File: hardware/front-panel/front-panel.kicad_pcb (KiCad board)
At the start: 4 copper layers, 180 x 100 mm, 78 parts, among them J1 Panel link 2x20 female, J10 SMA, J11 SMA, J12 SMA, J13 SMA, J14 SMA, J15 SMA, J16 SMA, J17 SMA, J18 SMA, J19 SMA, J2 Panel link 2x20 female, J20 SMA, J21 SMA, J22 SMA, J23 SMA, J24 SMA, J25 SMA, J26 SMA, J3 Panel link 2x20 female, J30 OLED 0.96in module on 1x4 soc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, J31 KF128-2.54-10P, J32 KF128-5.0-2P, J33 Qwiic (vertical), J40 Module header 2x6 (shrouded), J411 KF301-5.0-2P, J412 KF301-5.0-2P, Q411 MMBT5551, Q412 MMBT5551, Q421 MMBT5551, Q422 MMBT5551, U401 6N137S-TA1-L, U402 6N137S-TA1-L, U410 SN74AHCT541PWR

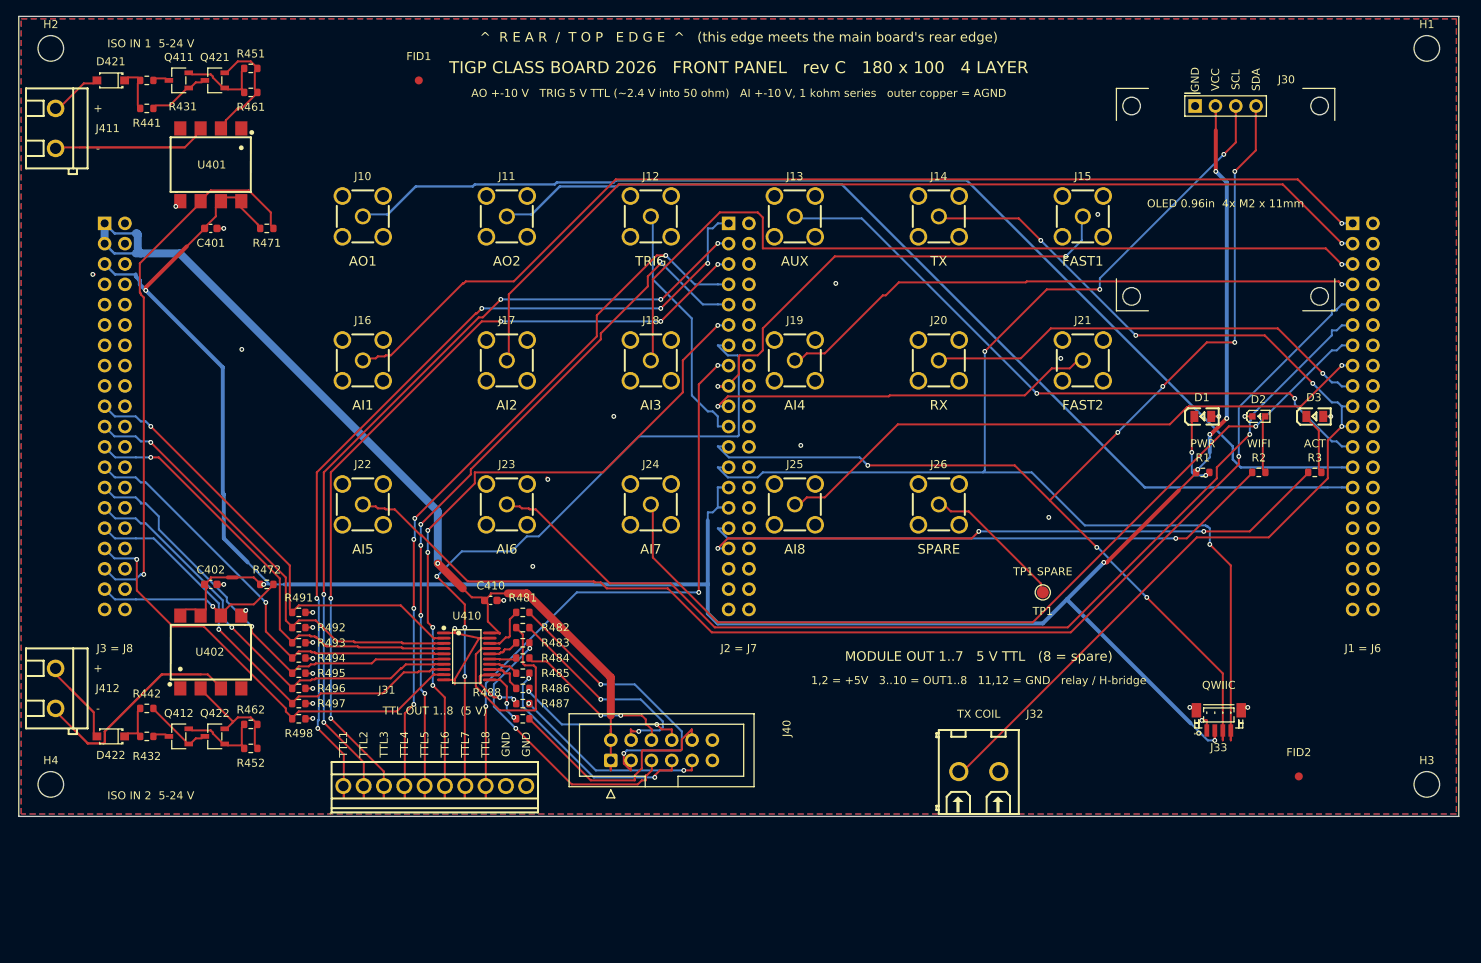
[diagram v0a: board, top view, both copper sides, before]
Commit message: front panel: OLED footprint per the real module (27 x 29 mm, holes 24 x 26 mm, header 1 mm below the top edge), panel + student copy regenerated, DRC 0/0 with zones filled
Co-Authored-By: Claude Fable 5.1 <noreply@anthropic.com>
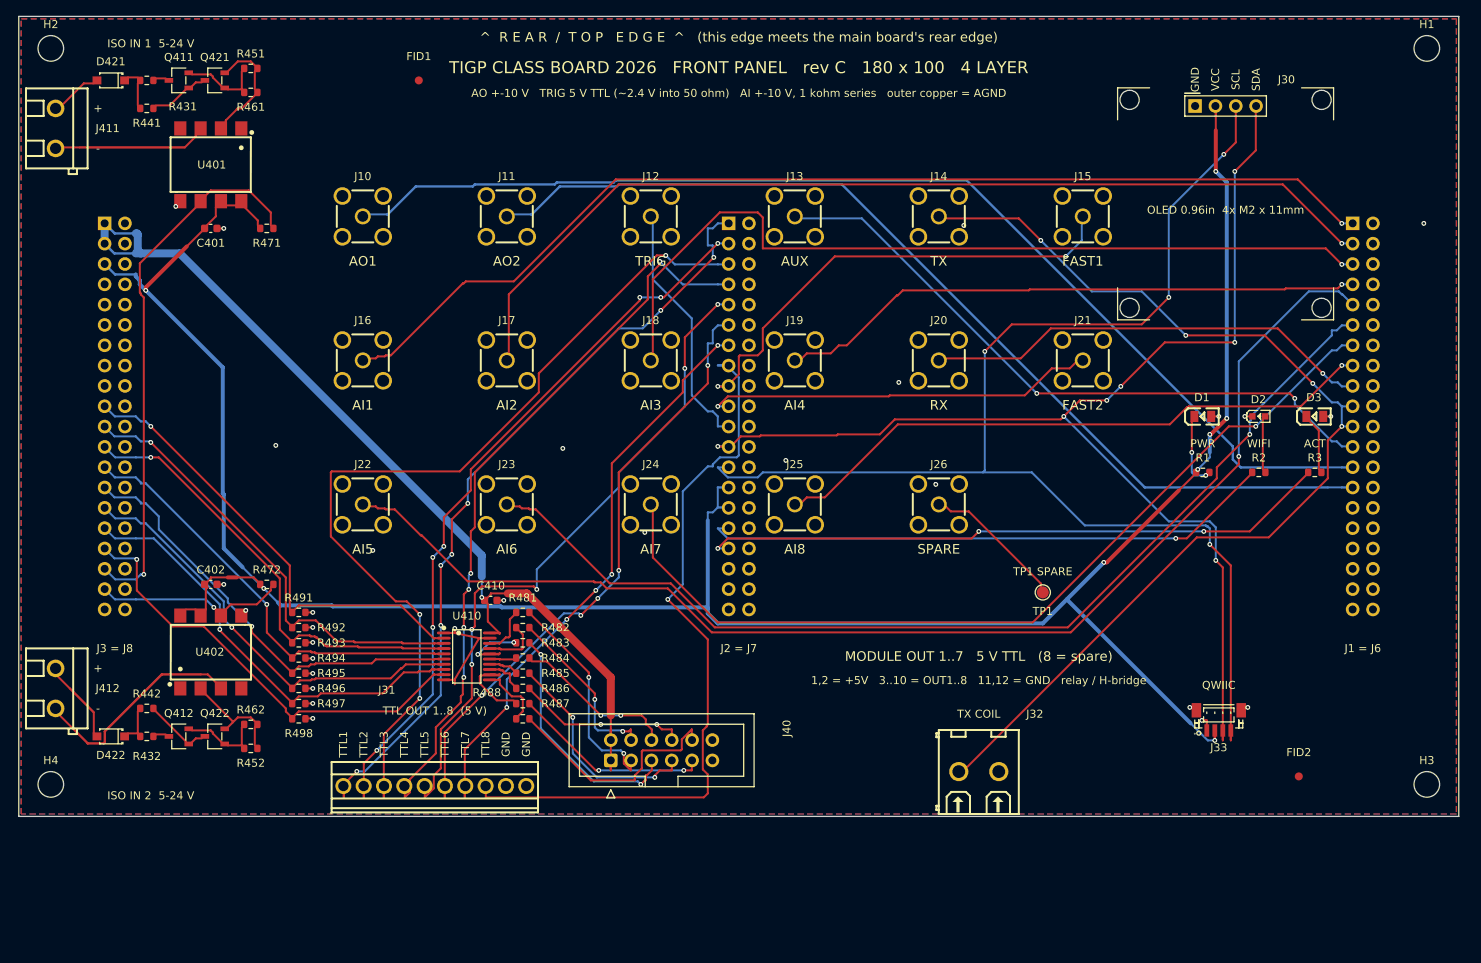
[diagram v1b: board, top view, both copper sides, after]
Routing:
- net /MODY2: track 28.8 -> 6.76 mm
- net TTL7: track 90.0 -> 72.4 mm, vias 3 -> 5
- net TTL8: track 77.7 -> 93.9 mm, vias 3 -> 1
- net TTL2: track 106.6 -> 92.1 mm, vias 5 -> 7
- net TTL1: track 110.6 -> 97.6 mm, vias 5 -> 7
- net /MODOUT1: track 38.3 -> 27.2 mm
- net TTL6: track 87.1 -> 77.9 mm
- net TTL5: track 91.9 -> 84.2 mm
- net I2C_SDA: track 148.0 -> 155.0 mm
- net TTL3: track 105.3 -> 112.2 mm, vias 5 -> 3
- net /MODOUT2: track 27.6 -> 21.6 mm
- net /MODY3: track 3.59 -> 9.27 mm, vias 0 -> 2
- net /MODOUT3: track 35.7 -> 30.0 mm
- net I2C_SCL: track 158.2 -> 163.8 mm
- net AI5: track 150.9 -> 155.3 mm
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
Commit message: front panel: male link headers J1/J2/J3 (Decision #62), J1 escapes outward; routed, DRC 0/0 with zones filled; student copy regenerated
Co-Authored-By: Claude Fable 5.1 <noreply@anthropic.com>
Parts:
- J1, J2, J3: value Panel link 2x20 female -> Panel link 2x20 male; footprint Connector_PinSocket_2.54mm:PinSocket_2x20_P2.54mm_Vertical -> Connector_PinHeader_2.54mm:PinHeader_2x20_P2.54mm_Vertical
- moved J1 2.54 mm to (169.3, 25.9)
- moved J3 2.54 mm to (13.3, 25.9)
- moved J2 2.54 mm to (91.3, 25.9)
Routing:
- net TX: track 131.8 -> 162.3 mm
- net AUX: track 81.1 -> 109.9 mm
- net I2C_SCL: track 163.8 -> 178.3 mm, vias 4 -> 6
- net RX: track 55.4 -> 69.9 mm, vias 1 -> 4
- net MOD2: track 56.6 -> 70.1 mm
- net TTL5: track 84.2 -> 92.0 mm
- net +5V_RAW: track 118.2 -> 112.3 mm
- net +3V3: track 298.4 -> 304.1 mm, vias 8 -> 7
- net AI4: track 72.7 -> 78.3 mm
- net I2C_SDA: track 155.0 -> 149.6 mm
- net AO2: track 122.1 -> 127.4 mm
- net AI8: track 76.0 -> 81.2 mm
- net AI3: track 105.2 -> 110.4 mm
- net AI2: track 121.6 -> 126.9 mm
- net AI1: track 134.4 -> 139.7 mm
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
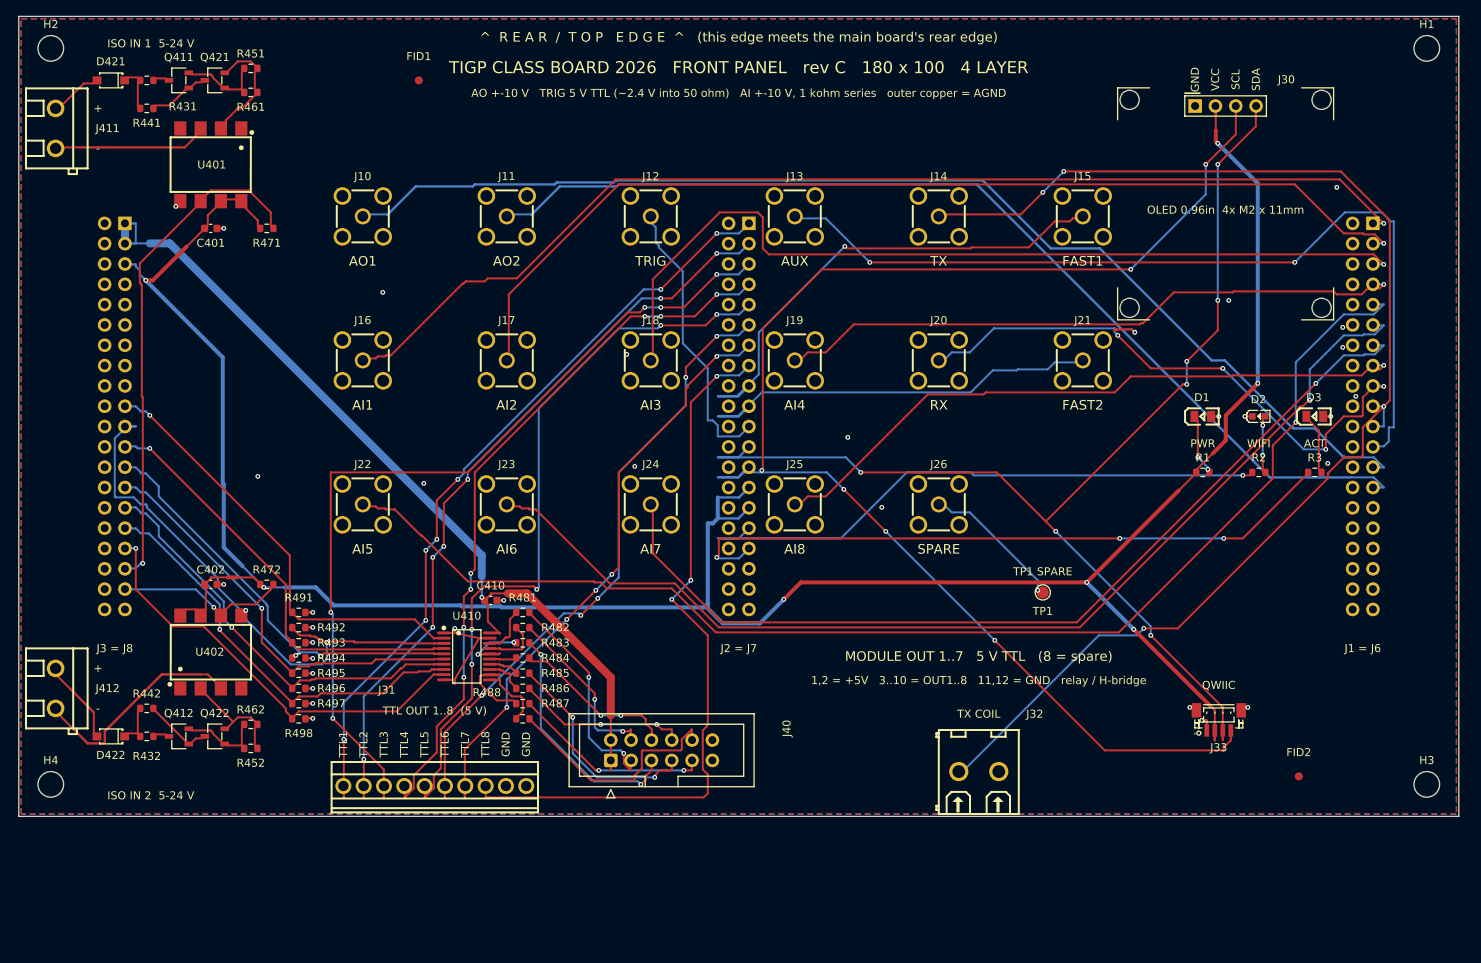
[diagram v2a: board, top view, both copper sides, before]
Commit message: Boards as hand-reworked by the instructor 2026-09-18 (Decision #66): three 2x20 links re-placed, jumpers -> headers, TCXO removed, 16 SMA; layout and routing in progress; review in the course repo notes
Co-Authored-By: Claude Fable 5.1 <noreply@anthropic.com>
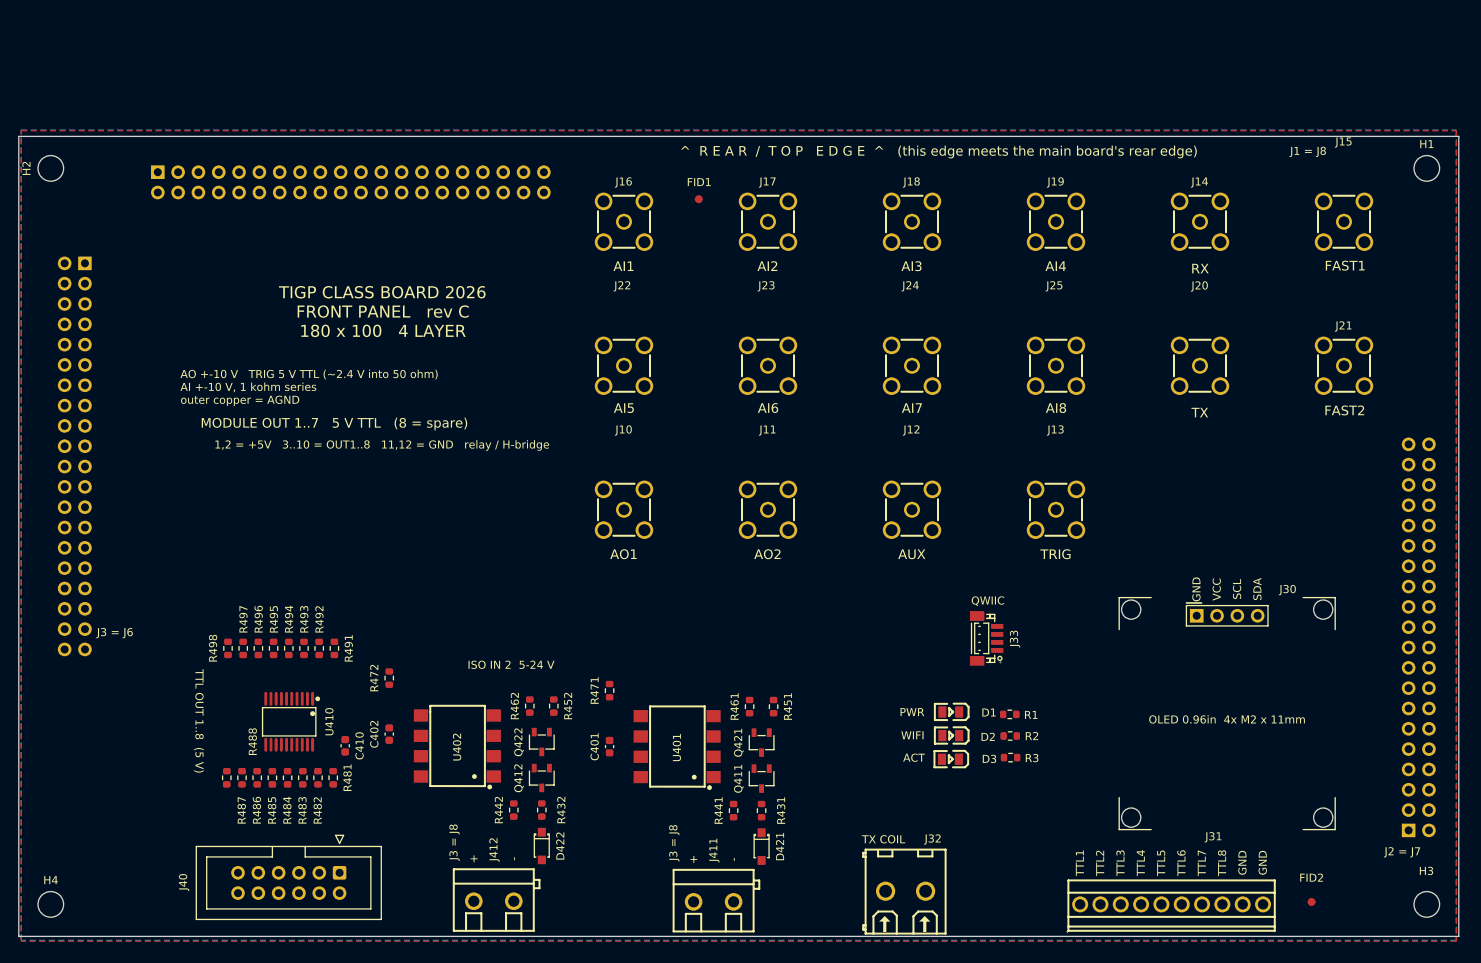
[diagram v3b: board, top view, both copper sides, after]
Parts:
- removed J26: SMA, class_board:SMA-TH_BWSMA-KE-Z001
- removed TP1: TP, class_board:TestPoint_Pad_D1.5mm
- D2: value YELLOW -> GREEN; footprint class_board:LED0603-RD-YELLOW -> class_board:LED0805-R-RD
- J1, J2, J3: value Panel link 2x20 male -> Conn_02x20_Odd_Even
- moved J1 152.0 mm to (17.4, 19.5), turned to -90 degrees
- moved J411 126.9 mm to (86.9, 110.7), turned to 0 degrees
- moved D421 125.7 mm to (92.9, 103.8), turned to -90 degrees
- moved R431 119.3 mm to (92.9, 99.3), turned to 90 degrees
- moved R441 114.4 mm to (89.4, 99.3), turned to 90 degrees
- moved Q411 113.7 mm to (92.9, 95.3), turned to 90 degrees
- moved J2 112.1 mm to (173.7, 101.8), turned to 0 degrees
- moved Q421 107.4 mm to (92.9, 90.8), turned to 90 degrees
- moved R451 103.1 mm to (94.4, 86.3), turned to 90 degrees
- moved R461 98.9 mm to (91.4, 86.3), turned to 90 degrees
- moved J31 93.3 mm to (144.1, 111.0)
- moved U401 93.2 mm to (82.3, 91.3), turned to 90 degrees
- moved C401 81.7 mm to (73.9, 91.3), turned to 90 degrees
- moved R471 71.9 mm to (73.9, 84.3), turned to 90 degrees
- moved J30 63.7 mm to (151.1, 74.9)
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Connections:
- J1 pad 1: AI1 -> AGND
- J1 pad 10: AGND -> unconnected-(J1-Pin_10-Pad10)
- J1 pad 11: AI6 -> AGND
- J1 pad 12: AGND -> /AUX
- J1 pad 13: AI7 -> AGND
- J1 pad 14: AGND -> unconnected-(J1-Pin_14-Pad14)
- J1 pad 15: AI8 -> AGND
- J1 pad 16: AGND -> /AO2
- J1 pad 17: RX -> AGND
- J1 pad 18: AGND -> /AO1
- J1 pad 19: TX -> AGND
- J1 pad 2: AGND -> unconnected-(J1-Pin_2-Pad2)
- J1 pad 20: AGND -> /TX
- J1 pad 21: TX -> AGND
- J1 pad 22: AGND -> /TX
- J1 pad 23: AUX -> AGND
- J1 pad 24: AGND -> /AI8
- J1 pad 25: AO1 -> AGND
- J1 pad 26: AGND -> /AI7
- J1 pad 27: AO2 -> AGND
- J1 pad 28: AGND -> /AI6
- J1 pad 29: (no net) -> AGND
- J1 pad 3: AI2 -> AGND
- J1 pad 30: AGND -> /AI5
- J1 pad 31: (no net) -> AGND
- J1 pad 32: AGND -> /RX
- J1 pad 33: (no net) -> AGND
- J1 pad 34: AGND -> /AI4
- J1 pad 35: (no net) -> AGND
- J1 pad 36: AGND -> /AI3
- J1 pad 37: (no net) -> AGND
- J1 pad 38: AGND -> /AI2
- J1 pad 39: (no net) -> AGND
- J1 pad 4: AGND -> unconnected-(J1-Pin_4-Pad4)
- J1 pad 40: AGND -> /AI1
- J1 pad 5: AI3 -> AGND
- J1 pad 6: AGND -> unconnected-(J1-Pin_6-Pad6)
- J1 pad 7: AI4 -> AGND
- J1 pad 8: AGND -> unconnected-(J1-Pin_8-Pad8)
- J1 pad 9: AI5 -> AGND
- J10 pad 5: AO1 -> /AO1
- J11 pad 5: AO2 -> /AO2
- J12 pad 5: TRIG_5V -> /TRIG_5V
- J13 pad 5: AUX -> /AUX
- J14 pad 5: TX -> /RX
- J15 pad 5: FASTTTL1 -> /FASTTTL1
- J16 pad 5: AI1 -> /AI1
- J17 pad 5: AI2 -> /AI2
- J18 pad 5: AI3 -> /AI3
- J19 pad 5: AI4 -> /AI4
- J2 pad 1: TTL1 -> /TTL8
- J2 pad 11: TTL6 -> /TTL3
- J2 pad 13: TTL7 -> /TTL2
- J2 pad 15: TTL8 -> /TTL1
- J2 pad 17: FASTTTL1 -> unconnected-(J2-Pin_17-Pad17)
- J2 pad 19: FASTTTL2 -> unconnected-(J2-Pin_19-Pad19)
- J2 pad 21: TRIG_5V -> unconnected-(J2-Pin_21-Pad21)
- J2 pad 23: I2C_SDA -> /LED_ACT
- J2 pad 25: I2C_SCL -> /LED_WIFI
- J2 pad 3: TTL2 -> /TTL7
- J2 pad 31: LED_WIFI -> /I2C_SCL
- J2 pad 33: LED_ACT -> /I2C_SDA
- J2 pad 35: (no net) -> /TRIG_5V
- J2 pad 37: (no net) -> /FASTTTL2
- J2 pad 39: (no net) -> /FASTTTL1
- J2 pad 5: TTL3 -> /TTL6
- J2 pad 7: TTL4 -> /TTL5
- J2 pad 9: TTL5 -> /TTL4
- J20 pad 5: RX -> /TX
- J21 pad 5: FASTTTL2 -> /FASTTTL2
- J22 pad 5: AI5 -> /AI5
- J23 pad 5: AI6 -> /AI6
- J24 pad 5: AI7 -> /AI7
- J25 pad 5: AI8 -> /AI8
- J3 pad 11: GPIO7 -> unconnected-(J3-Pin_11-Pad11)
- J3 pad 13: GPIO15 -> unconnected-(J3-Pin_13-Pad13)
- J3 pad 15: GPIO43 -> /OPTO_IN1
- J3 pad 17: GPIO44 -> /OPTO_IN2
- J3 pad 19: MOD1 -> unconnected-(J3-Pin_19-Pad19)
- J3 pad 21: MOD2 -> unconnected-(J3-Pin_21-Pad21)
- J3 pad 23: MOD3 -> /MOD1
- J3 pad 25: MOD4 -> /MOD2
- J3 pad 27: MOD5 -> /MOD3
- J3 pad 29: MOD6 -> /MOD4
- J3 pad 31: MOD7 -> /MOD5
- J3 pad 33: MOD8 -> /MOD6
- J3 pad 35: OPTO_IN1 -> /MOD7
- J3 pad 37: OPTO_IN2 -> unconnected-(J3-Pin_37-Pad37)
- J3 pad 39: (no net) -> unconnected-(J3-Pin_39-Pad39)
- J3 pad 7: GPIO4 -> unconnected-(J3-Pin_7-Pad7)
- J3 pad 9: GPIO6 -> unconnected-(J3-Pin_9-Pad9)
- J30 pad 3: I2C_SCL -> /I2C_SCL
- J30 pad 4: I2C_SDA -> /I2C_SDA
- J31 pad 1: TTL1 -> /TTL1
- J31 pad 2: TTL2 -> /TTL2
- J31 pad 3: TTL3 -> /TTL3
- J31 pad 4: TTL4 -> /TTL4
- J31 pad 5: TTL5 -> /TTL5
- J31 pad 6: TTL6 -> /TTL6
- J31 pad 7: TTL7 -> /TTL7
- J31 pad 8: TTL8 -> /TTL8
- J32 pad 1: TX -> /TX
- J33 pad 3: I2C_SDA -> /I2C_SDA
- J33 pad 4: I2C_SCL -> /I2C_SCL
- R2 pad 1: LED_WIFI -> /LED_WIFI
- R3 pad 1: LED_ACT -> /LED_ACT
- R471 pad 2: OPTO_IN1 -> /OPTO_IN1
- R472 pad 2: OPTO_IN2 -> /OPTO_IN2
- R491 pad 1: MOD1 -> /MOD1
- R492 pad 1: MOD2 -> /MOD2
- R493 pad 1: MOD3 -> /MOD3
- R494 pad 1: MOD4 -> /MOD4
- R495 pad 1: MOD5 -> /MOD5
- R496 pad 1: MOD6 -> /MOD6
- R497 pad 1: MOD7 -> /MOD7
- R498 pad 1: MOD8 -> /MOD8
- U401 pad 1: (no net) -> unconnected-(U401-NC-Pad1)
- U401 pad 4: (no net) -> unconnected-(U401-NC-Pad4)
- U401 pad 6: OPTO_IN1 -> /OPTO_IN1
- U402 pad 1: (no net) -> unconnected-(U402-NC-Pad1)
- U402 pad 4: (no net) -> unconnected-(U402-NC-Pad4)
- U402 pad 6: OPTO_IN2 -> /OPTO_IN2
- U410 pad 2: MOD1 -> /MOD1
- U410 pad 3: MOD2 -> /MOD2
- U410 pad 4: MOD3 -> /MOD3
- U410 pad 5: MOD4 -> /MOD4
- U410 pad 6: MOD5 -> /MOD5
- U410 pad 7: MOD6 -> /MOD6
- U410 pad 8: MOD7 -> /MOD7
- U410 pad 9: MOD8 -> /MOD8
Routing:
- net +3V3: track 304.1 -> 0.00 mm, vias 7 -> 0
- net I2C_SCL: track 178.3 -> 0.00 mm, vias 6 -> 0
- net TX: track 162.3 -> 0.00 mm, vias 4 -> 0
- net AI5: track 158.4 -> 0.00 mm, vias 1 -> 0
- net I2C_SDA: track 149.6 -> 0.00 mm, vias 7 -> 0
- net AO1: track 144.7 -> 0.00 mm
- net AI1: track 139.7 -> 0.00 mm, vias 1 -> 0
- net AI6: track 134.4 -> 0.00 mm, vias 1 -> 0
- net AO2: track 127.4 -> 0.00 mm
- net AI2: track 126.9 -> 0.00 mm, vias 1 -> 0
- net AI7: track 115.9 -> 0.00 mm, vias 1 -> 0
- net +5V_RAW: track 112.3 -> 0.00 mm, vias 1 -> 0
- net AI3: track 110.4 -> 0.00 mm, vias 1 -> 0
- net AUX: track 109.9 -> 0.00 mm, vias 2 -> 0
- net TTL3: track 107.9 -> 0.00 mm, vias 5 -> 0
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- added copper zone on B.Cu, net GND
- removed copper zone on B.Cu, net AGND
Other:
- board text added: "J1 = J8"
- board text added: "J3"
- board text added: "J3 = J6"
- board text removed: "ISO IN 1 5-24 V"
- board text removed: "J1 = J6"
- board text removed: "J3 pin 1"
- board text removed: "SPARE"
- board text removed: "TP1 SPARE"
